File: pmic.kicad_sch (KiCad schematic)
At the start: 61 parts, among them J401 EMI shield frame, U401 STPMIC1DPQR

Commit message: Clean up schematics
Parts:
- removed R410: 0 Ω, perfect_footprints:R_0201_0603Metric, symbol Device:R
- renumbered R411 to R410, TP403 to TP402, TP404 to TP403, TP405 to TP404, TP406 to TP405, TP407 to TP406, TP402 to TP407
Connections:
- net PONKEY_N: now also TP407.1
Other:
- moved on the sheet: TP401, TP407
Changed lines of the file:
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@@
 	(title_block
 		(title "Linux SBC")
-		(date "2025-12-19")
+		(date "2025-12-26")
 		(rev "v1.0.0")
 	)
@@
 	)
 	(junction
+		(at 87.63 208.28)
+		(diameter 0)
+		(color 0 0 0 0)
+	)
+	(junction
 		(at 109.22 195.58)
 		(diameter 0)
@@
 	)
 	(junction
-		(at 80.01 208.28)
-		(diameter 0)
-		(color 0 0 0 0)
-	)
-	(junction
 		(at 110.49 198.12)
 		(diameter 0)
@@
 	(wire
 		(pts
+			(xy 87.63 208.28) (xy 83.82 208.28)
+		)
+		(stroke
+			(width 0)
+			(type default)
+		)
+	)
+	(wire
+		(pts
 			(xy 254 129.54) (xy 254 138.43)
 		)
@@
 	(wire
 		(pts
-			(xy 87.63 205.74) (xy 87.63 210.82)
-		)
-		(stroke
-			(width 0)
-			(type default)
-		)
-	)
-	(wire
-		(pts
 			(xy 160.02 182.88) (xy 162.56 182.88)
 		)
@@
 	(wire
 		(pts
-			(xy 138.43 205.74) (xy 162.56 205.74)
+			(xy 228.6 147.32) (xy 241.3 147.32)
 		)
 		(stroke
@@
 	(wire
 		(pts
-			(xy 228.6 147.32) (xy 241.3 147.32)
+			(xy 147.32 205.74) (xy 162.56 205.74)
 		)
 		(stroke
@@
 	(wire
 		(pts
+			(xy 147.32 205.74) (xy 147.32 210.82)
+		)
+		(stroke
+			(width 0)
+			(type default)
+		)
+	)
+	(wire
+		(pts
 			(xy 68.58 200.66) (xy 96.52 200.66)
 		)
@@
 	(wire
 		(pts
-			(xy 80.01 208.28) (xy 83.82 208.28)
-		)
-		(stroke
-			(width 0)
-			(type default)
-		)
-	)
-	(wire
-		(pts
 			(xy 254 147.32) (xy 266.7 147.32)
 		)
@@
 	(wire
 		(pts
+			(xy 87.63 208.28) (xy 130.81 208.28)
+		)
+		(stroke
+			(width 0)
+			(type default)
+		)
+	)
+	(wire
+		(pts
 			(xy 138.43 200.66) (xy 162.56 200.66)
 		)
@@
 	(wire
 		(pts
-			(xy 68.58 208.28) (xy 80.01 208.28)
+			(xy 68.58 208.28) (xy 83.82 208.28)
 		)
 		(stroke
@@
 	(wire
 		(pts
-			(xy 83.82 208.28) (xy 130.81 208.28)
-		)
-		(stroke
-			(width 0)
-			(type default)
-		)
-	)
-	(wire
-		(pts
 			(xy 83.82 176.53) (xy 96.52 176.53)
 		)
@@
 	(wire
 		(pts
-			(xy 80.01 208.28) (xy 80.01 210.82)
-		)
-		(stroke
-			(width 0)
-			(type default)
-		)
-	)
-	(wire
-		(pts
-			(xy 87.63 205.74) (xy 130.81 205.74)
+			(xy 87.63 208.28) (xy 87.63 210.82)
 		)
 		(stroke
@@
 		(on_board yes)
 		(dnp no)
-		(property "Reference" "TP407"
+		(property "Reference" "TP406"
 			(at 125.73 215.138 0)
 			(effects
@@
 			(project "linux-sbc"
 				(path "/fa11a02f-8043-4153-ab69-88d766503017/b1491768-4eca-4c4e-8d13-68e94666bd26"
-					(reference "TP407")
+					(reference "TP406")
 					(unit 1)
 				)
@@
 		(on_board yes)
 		(dnp no)
-		(property "Reference" "TP406"
+		(property "Reference" "TP405"
 			(at 118.11 215.138 0)
 			(effects
@@
 			(project "linux-sbc"
 				(path "/fa11a02f-8043-4153-ab69-88d766503017/b1491768-4eca-4c4e-8d13-68e94666bd26"
-					(reference "TP406")
+					(reference "TP405")
 					(unit 1)
 				)
@@
 		(on_board yes)
 		(dnp no)
-		(property "Reference" "TP404"
+		(property "Reference" "TP403"
 			(at 102.87 215.138 0)
 			(effects
@@
 			(project "linux-sbc"
 				(path "/fa11a02f-8043-4153-ab69-88d766503017/b1491768-4eca-4c4e-8d13-68e94666bd26"
-					(reference "TP404")
+					(reference "TP403")
 					(unit 1)
 				)
@@
 		(on_board yes)
 		(dnp no)
-		(property "Reference" "R411"
+		(property "Reference" "R410"
 			(at 131.826 208.026 90)
 			(effects
@@
 			(project "linux-sbc"
 				(path "/fa11a02f-8043-4153-ab69-88d766503017/b1491768-4eca-4c4e-8d13-68e94666bd26"
-					(reference "R411")
+					(reference "R410")
 					(unit 1)
 				)
@@
 	(symbol
 		(lib_id "Connector:TestPoint")
-		(at 80.01 210.82 0)
+		(at 87.63 210.82 0)
 		(mirror x)
 		(unit 1)
@@
 		(dnp no)
 		(property "Reference" "TP401"
-			(at 80.01 215.138 0)
+			(at 87.63 215.138 0)
 			(effects
 				(font
@@
 		)
 		(property "Value" "TestPoint"
-			(at 82.55 214.122 90)
+			(at 90.17 214.122 90)
 			(effects
 				(font
@@
 		)
 		(property "Footprint" "TestPoint:TestPoint_Pad_D1.0mm"
-			(at 85.09 210.82 0)
+			(at 92.71 210.82 0)
 			(effects
 				(font
@@
 		)
 		(property "Datasheet" "~"
-			(at 85.09 210.82 0)
+			(at 92.71 210.82 0)
 			(effects
 				(font
@@
 		)
 		(property "Description" "test point"
-			(at 80.01 210.82 0)
+			(at 87.63 210.82 0)
 			(effects
 				(font
@@
 	)
 	(symbol
-		(lib_name "R_1")
-		(lib_id "Device:R")
-		(at 134.62 205.74 90)
-		(mirror x)
-		(unit 1)
-		(exclude_from_sim no)
-		(in_bom yes)
-		(on_board yes)
-		(dnp no)
-		(property "Reference" "R410"
-			(at 131.826 205.486 90)
-			(effects
-				(font
-					(size 1.27 1.27)
-				)
-				(justify left bottom)
-			)
-		)
-		(property "Value" "0 Ω"
-			(at 137.414 205.486 90)
-			(effects
-				(font
-					(size 1.27 1.27)
-				)
-				(justify right bottom)
-			)
-		)
-		(property "Footprint" "perfect_footprints:R_0201_0603Metric"
-			(at 134.62 203.962 90)
-			(effects
-				(font
-					(size 1.27 1.27)
-				)
-				(hide yes)
-			)
-		)
-		(property "Datasheet" "https://industrial.panasonic.com/ww/products/pt/general-purpose-chip-resistors/models/ERJ1GN0R00C"
-			(at 134.62 205.74 0)
-			(effects
-				(font
-					(size 1.27 1.27)
-				)
-				(hide yes)
-			)
-		)
-		(property "Description" "0 Ohms Jumper Chip Resistor 0201 (0603 Metric) Thick Film"
-			(at 134.62 205.74 0)
-			(effects
-				(font
-					(size 1.27 1.27)
-				)
-				(hide yes)
-			)
-		)
-		(property "MPN" "ERJ-1GN0R00C"
-			(at 134.62 205.74 0)
-			(effects
-				(font
-					(size 1.27 1.27)
-				)
-				(hide yes)
-			)
-		)
-		(property "Manufacturer" "Panasonic Electronic Components"
-			(at 134.62 205.74 0)
-			(effects
-				(font
-					(size 1.27 1.27)
-				)
-				(hide yes)
-			)
-		)
-		(property "Size" "0201"
-			(at 141.478 205.486 90)
-			(effects
-				(font
-					(size 0.7 0.7)
-				)
-				(justify right bottom)
-			)
-		)
-		(property "Digi-Key Part Number" "P15979CT-ND"
-			(at 134.62 205.74 90)
-			(effects
-				(font
-					(size 1.27 1.27)
-				)
-				(hide yes)
-			)
-		)
-		(pin "2"
-		)
-		(pin "1"
-		)
-		(instances
-			(project "linux-sbc"
-				(path "/fa11a02f-8043-4153-ab69-88d766503017/b1491768-4eca-4c4e-8d13-68e94666bd26"
-					(reference "R410")
-					(unit 1)
-				)
-			)
-		)
-	)
-	(symbol
 		(lib_id "Device:C")
 		(at 292.1 190.5 0)
@@
 		(on_board yes)
 		(dnp no)
-		(property "Reference" "TP405"
+		(property "Reference" "TP404"
 			(at 110.49 215.138 0)
 			(effects
@@
 			(project "linux-sbc"
 				(path "/fa11a02f-8043-4153-ab69-88d766503017/b1491768-4eca-4c4e-8d13-68e94666bd26"
-					(reference "TP405")
+					(reference "TP404")
 					(unit 1)
 				)
@@
 	(symbol
 		(lib_id "Connector:TestPoint")
-		(at 87.63 210.82 0)
+		(at 147.32 210.82 0)
 		(mirror x)
 		(unit 1)
@@
 		(on_board yes)
 		(dnp no)
-		(property "Reference" "TP402"
-			(at 87.63 215.138 0)
+		(property "Reference" "TP407"
+			(at 147.32 215.138 0)
 			(effects
 				(font
@@
 		)
 		(property "Value" "TestPoint"
-			(at 90.17 214.122 90)
+			(at 149.86 214.122 90)
 			(effects
 				(font
@@
 		)
 		(property "Footprint" "TestPoint:TestPoint_Pad_D1.0mm"
-			(at 92.71 210.82 0)
+			(at 152.4 210.82 0)
 			(effects
 				(font
@@
 		)
 		(property "Datasheet" "~"
-			(at 92.71 210.82 0)
+			(at 152.4 210.82 0)
 			(effects
 				(font
@@
 		)
 		(property "Description" "test point"
-			(at 87.63 210.82 0)
+			(at 147.32 210.82 0)
 			(effects
 				(font
@@
 			(project "linux-sbc"
 				(path "/fa11a02f-8043-4153-ab69-88d766503017/b1491768-4eca-4c4e-8d13-68e94666bd26"
-					(reference "TP402")
+					(reference "TP407")
 					(unit 1)
 				)
@@
 		(on_board yes)
 		(dnp no)
-		(property "Reference" "TP403"
+		(property "Reference" "TP402"
 			(at 95.25 215.138 0)
 			(effects
@@
 			(project "linux-sbc"
 				(path "/fa11a02f-8043-4153-ab69-88d766503017/b1491768-4eca-4c4e-8d13-68e94666bd26"
-					(reference "TP403")
+					(reference "TP402")
 					(unit 1)
 				)

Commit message: Layout the PMIC
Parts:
- C403, C405, C407, C408, C410, C411, C412, C414, C416, C418, C420, C422, C424: footprint Capacitor_SMD:C_0603_1608Metric -> perfect_footprints:C_0402_1005Metric; Digi-Key Part Number 490-7205-1-ND -> 1276-6836-1-ND; MPN GRM188R6YA475KE15D -> CL05A475MO5NUNC; Manufacturer Murata Electronics -> Samsung Electro-Mechanics; Size 0603 -> 0402; Voltage rating 35 V -> 16 V

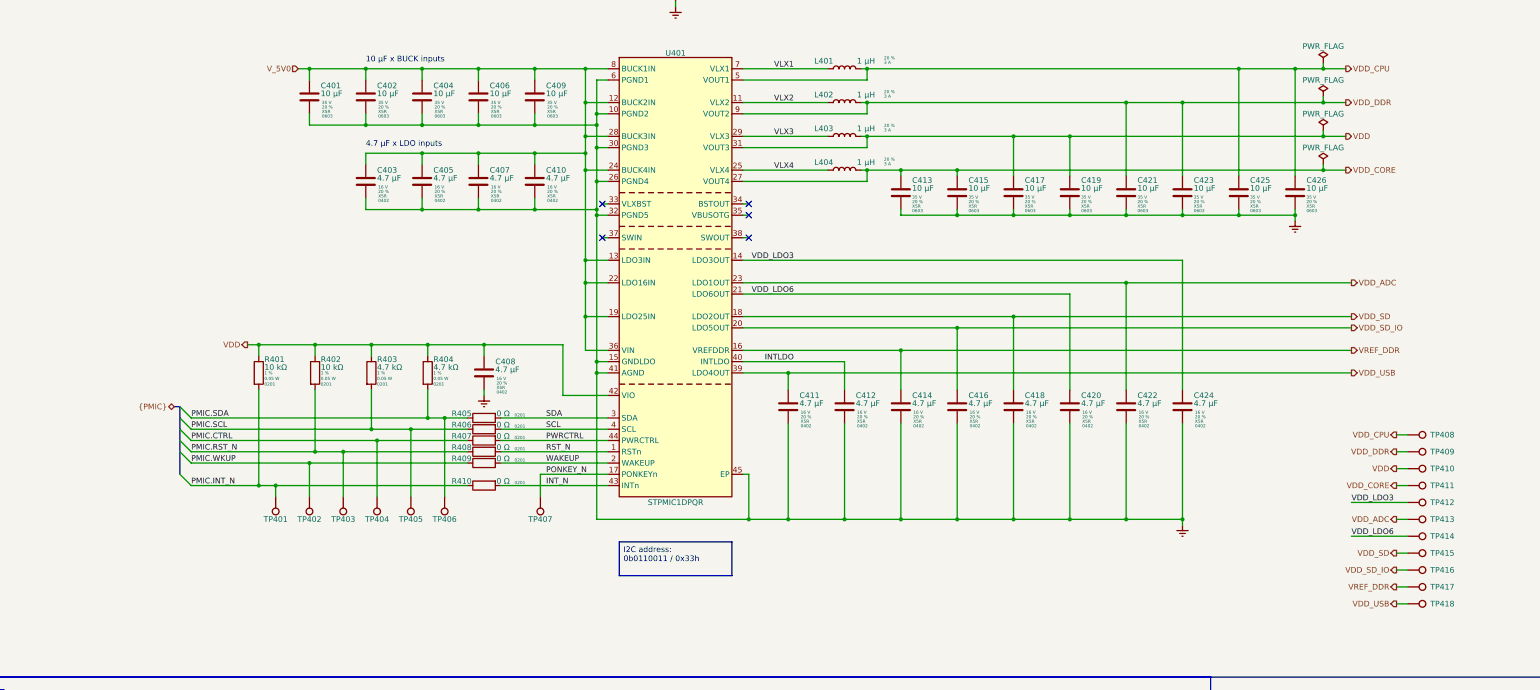
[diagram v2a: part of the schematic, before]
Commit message: Remove redundant test points, fix layouts
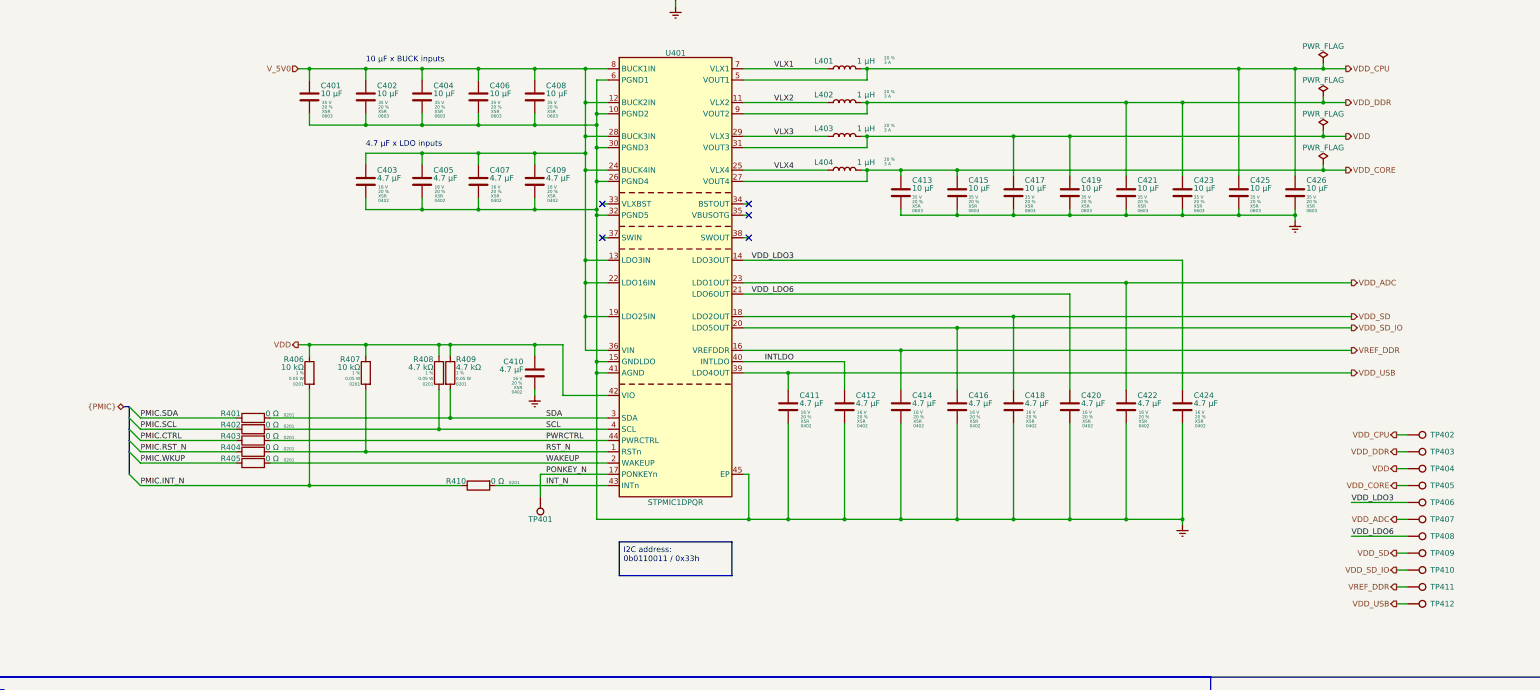
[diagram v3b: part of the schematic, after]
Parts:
- removed TP401, TP402, TP403, TP404, TP405, TP406: TestPoint, TestPoint:TestPoint_Pad_D1.0mm, symbol Connector:TestPoint
- renumbered C409 to C408, C410 to C409, C408 to C410, R405 to R401, R406 to R402, R407 to R403, R408 to R404, R409 to R405, R401 to R406, R402 to R407, R403 to R408, R404 to R409, TP407 to TP401, TP408 to TP402, TP409 to TP403, TP410 to TP404, TP411 to TP405, TP412 to TP406, TP413 to TP407, TP414 to TP408, TP415 to TP409, TP416 to TP410, TP417 to TP411, TP418 to TP412
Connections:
- net PMIC.RST_N: no longer R407.2
- net PMIC.SCL: no longer R408.2
- net PMIC.SDA: no longer R409.2
- net RST_N: now also R407.2
- net SCL: now also R408.2
- net SDA: now also R409.2
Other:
- moved on the sheet: C410, R401, R402, R403, R404, R405, R406, R407, R408, R409, R410

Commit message: Update 0402 footprints
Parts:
- C403, C405, C407, C409, C410, C411, C412, C414, C416, C418, C420, C422, C424: footprint perfect_footprints:C_0402_1005Metric -> perfect_footprints:C_0402_1005Metric_HDI
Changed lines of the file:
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@@
 			)
 		)
-		(property "Footprint" "perfect_footprints:C_0402_1005Metric"
+		(property "Footprint" "perfect_footprints:C_0402_1005Metric_HDI"
 			(at 216.8652 194.31 0)
 			(effects
@@
 			)
 		)
-		(property "Footprint" "perfect_footprints:C_0402_1005Metric"
+		(property "Footprint" "perfect_footprints:C_0402_1005Metric_HDI"
 			(at 254.9652 194.31 0)
 			(effects
@@
 			)
 		)
-		(property "Footprint" "perfect_footprints:C_0402_1005Metric"
+		(property "Footprint" "perfect_footprints:C_0402_1005Metric_HDI"
 			(at 229.5652 194.31 0)
 			(effects
@@
 			)
 		)
-		(property "Footprint" "perfect_footprints:C_0402_1005Metric"
+		(property "Footprint" "perfect_footprints:C_0402_1005Metric_HDI"
 			(at 147.0152 143.51 0)
 			(effects
@@
 			)
 		)
-		(property "Footprint" "perfect_footprints:C_0402_1005Metric"
+		(property "Footprint" "perfect_footprints:C_0402_1005Metric_HDI"
 			(at 280.3652 194.31 0)
 			(effects
@@
 			)
 		)
-		(property "Footprint" "perfect_footprints:C_0402_1005Metric"
+		(property "Footprint" "perfect_footprints:C_0402_1005Metric_HDI"
 			(at 242.2652 194.31 0)
 			(effects
@@
 			)
 		)
-		(property "Footprint" "perfect_footprints:C_0402_1005Metric"
+		(property "Footprint" "perfect_footprints:C_0402_1005Metric_HDI"
 			(at 108.9152 143.51 0)
 			(effects
@@
 			)
 		)
-		(property "Footprint" "perfect_footprints:C_0402_1005Metric"
+		(property "Footprint" "perfect_footprints:C_0402_1005Metric_HDI"
 			(at 267.6652 194.31 0)
 			(effects
@@
 			)
 		)
-		(property "Footprint" "perfect_footprints:C_0402_1005Metric"
+		(property "Footprint" "perfect_footprints:C_0402_1005Metric_HDI"
 			(at 121.6152 143.51 0)
 			(effects
@@
 			)
 		)
-		(property "Footprint" "perfect_footprints:C_0402_1005Metric"
+		(property "Footprint" "perfect_footprints:C_0402_1005Metric_HDI"
 			(at 134.3152 143.51 0)
 			(effects
@@
 			)
 		)
-		(property "Footprint" "perfect_footprints:C_0402_1005Metric"
+		(property "Footprint" "perfect_footprints:C_0402_1005Metric_HDI"
 			(at 145.0848 186.69 0)
 			(effects
@@
 			)
 		)
-		(property "Footprint" "perfect_footprints:C_0402_1005Metric"
+		(property "Footprint" "perfect_footprints:C_0402_1005Metric_HDI"
 			(at 293.0652 194.31 0)
 			(effects
@@
 			)
 		)
-		(property "Footprint" "perfect_footprints:C_0402_1005Metric"
+		(property "Footprint" "perfect_footprints:C_0402_1005Metric_HDI"
 			(at 204.1652 194.31 0)
 			(effects

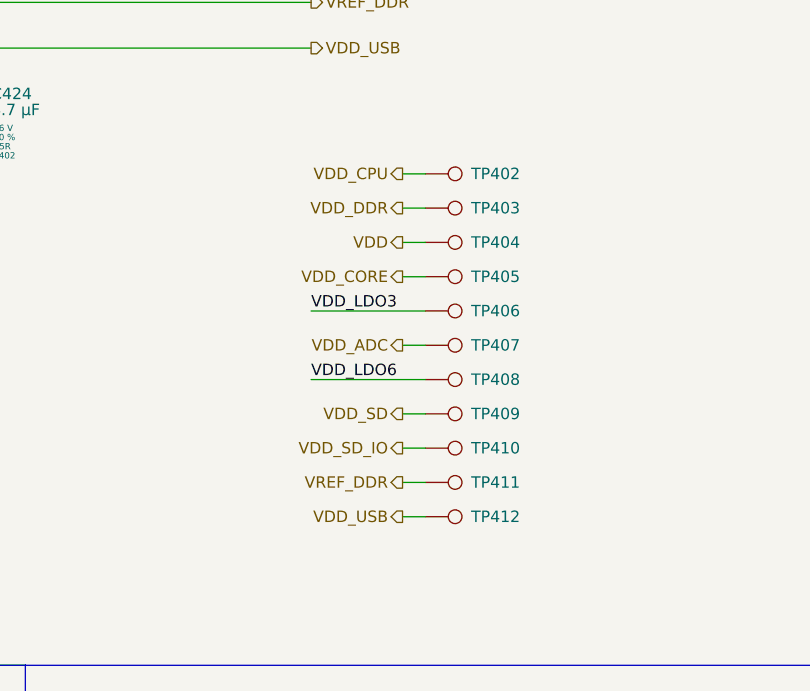
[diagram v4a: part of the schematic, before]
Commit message: Remove redundant test points and add bottom silkscreen
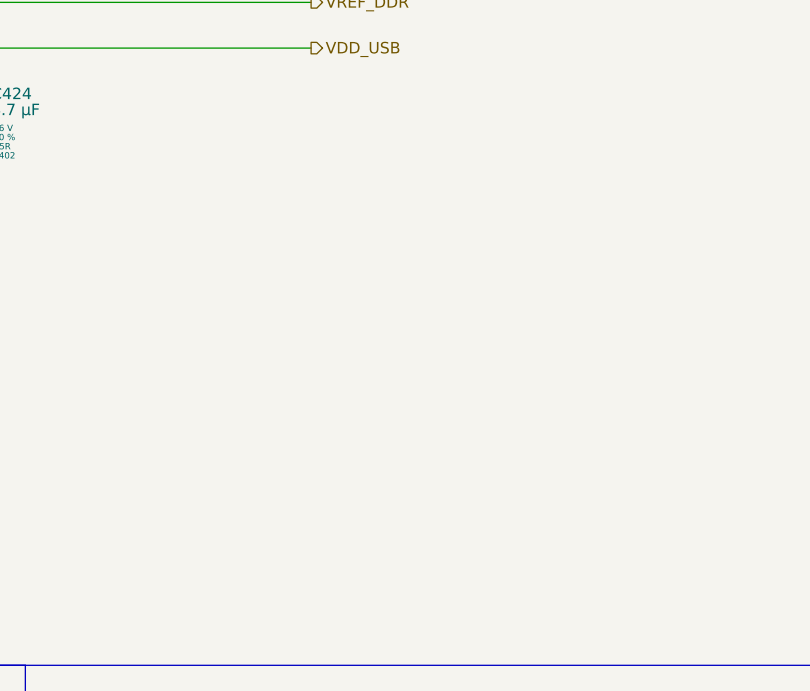
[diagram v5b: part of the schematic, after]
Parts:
- removed TP402, TP403, TP404, TP405, TP406, TP407, TP408, TP409, TP410, TP411, TP412: TestPoint, TestPoint:TestPoint_Pad_D1.0mm, symbol Connector:TestPoint
